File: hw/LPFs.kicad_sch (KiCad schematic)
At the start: 21 parts, among them U201 AS183-92LF, U202 AS183-92LF, U203 AS183-92LF, U204 AS183-92LF

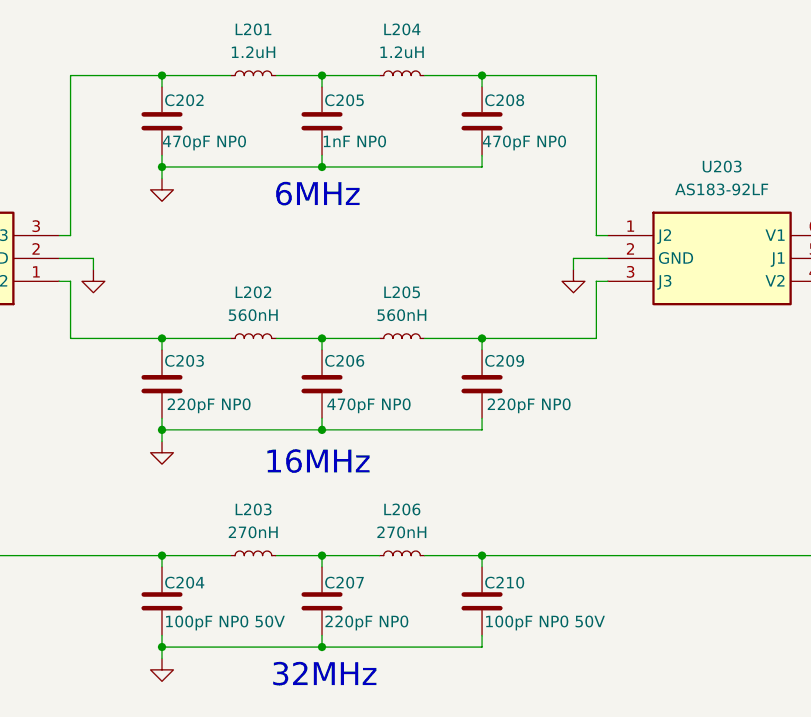
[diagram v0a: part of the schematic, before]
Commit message: Parts ordered for DVT1 build
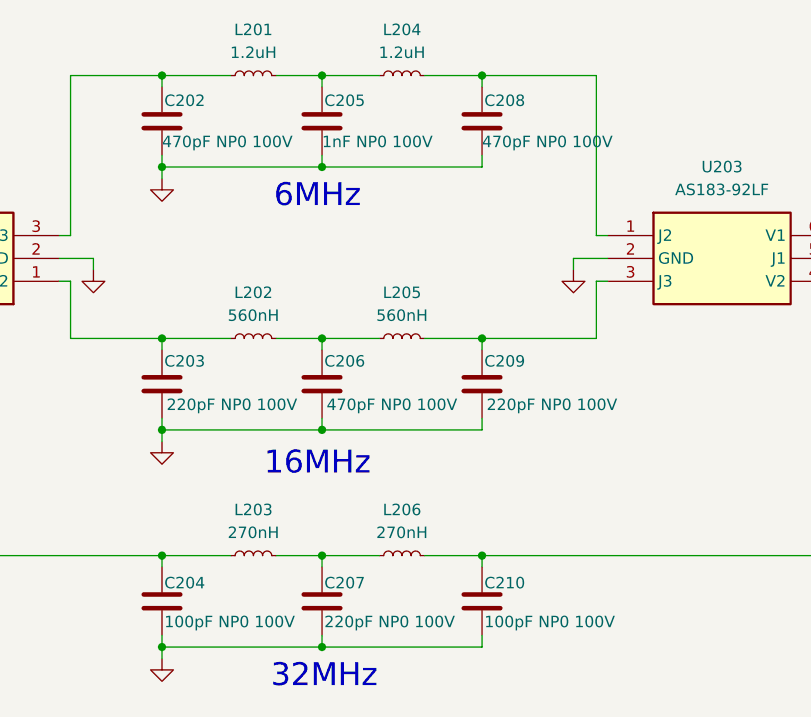
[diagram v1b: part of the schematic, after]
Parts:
- C201, C211: MFG (none) -> Kyocera AVX; MPN (none) -> KGM15BR71H104KT; Mouser_PN (none) -> 581-KGM15BR71H104KT
- C202, C206, C208: value 470pF NP0 -> 470pF NP0 100V; footprint Capacitor_SMD:C_0402_1005Metric -> Capacitor_SMD:C_0603_1608Metric; MFG (none) -> muRata; MPN (none) -> GCM1885C2A471FA6D; Mouser_PN (none) -> 81-GCM1885C2A471FA6D
- C203, C207, C209: value 220pF NP0 -> 220pF NP0 100V; footprint Capacitor_SMD:C_0402_1005Metric -> Capacitor_SMD:C_0603_1608Metric; MFG (none) -> muRata; MPN (none) -> GCM1885C2A221FA6D; Mouser_PN (none) -> 81-GCM1885C2A221FA6D
- C204, C210: value 100pF NP0 50V -> 100pF NP0 100V; footprint Capacitor_SMD:C_0402_1005Metric -> Capacitor_SMD:C_0603_1608Metric; MFG (none) -> Kyocera AVX; MPN (none) -> KGM15ACG2A101FT; Mouser_PN (none) -> 581-KGM15ACG2A101FT
- C205: value 1nF NP0 -> 1nF NP0 100V; footprint Capacitor_SMD:C_0402_1005Metric -> Capacitor_SMD:C_0603_1608Metric; MFG (none) -> Kyocera AVX; MPN (none) -> KGM15ACG2A102FT; Mouser_PN (none) -> 581-KGM15ACG2A102FT
- L201, L204: MFG (none) -> Bourns; MPN (none) -> CW252016-1R2J; Mouser_PN (none) -> 652-CW252016-1R2J
- L202, L205: footprint Inductor_SMD:L_0805_2012Metric -> Inductor_SMD:L_1008_2520Metric; MFG (none) -> muRata; MPN (none) -> LQW2UASR56G00L; Mouser_PN (none) -> 81-LQW2UASR56G00L
- L203, L206: MFG (none) -> Bourns; MPN (none) -> CW252016-R27J; Mouser_PN (none) -> 652-CW252016-R27J
- U201, U202, U203, U204: MFG (none) -> Skyworks; Mouser_PN (none) -> 873-AS183-92LF
